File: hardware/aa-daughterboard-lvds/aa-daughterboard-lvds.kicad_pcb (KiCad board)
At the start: 4 copper layers, 175.3 x 96.5 mm, 162 parts, among them CN1 Barrel_Jack, CN10 6P6C, CN11 6P6C, CN12 6P6C, CN13 6P6C, CN14 Conn_01x08, CN15 Conn_01x08, CN16 Conn_01x08, CN17 8P8C, CN18 8P8C, CN19 8P8C, CN2 Conn_01x02, CN3 Conn_01x06, CN4 Conn_01x06, CN5 6P6C, CN6 Conn_01x04, CN7 Conn_01x04, CN8 Conn_01x04, CN9 Conn_01x04, U1 24LC08, U2 NIS5132xx, U3 uA7805, U4 75ALS192, U5 75ALS192, U6 75ALS192, U7 75ALS192, U8 75ALS192

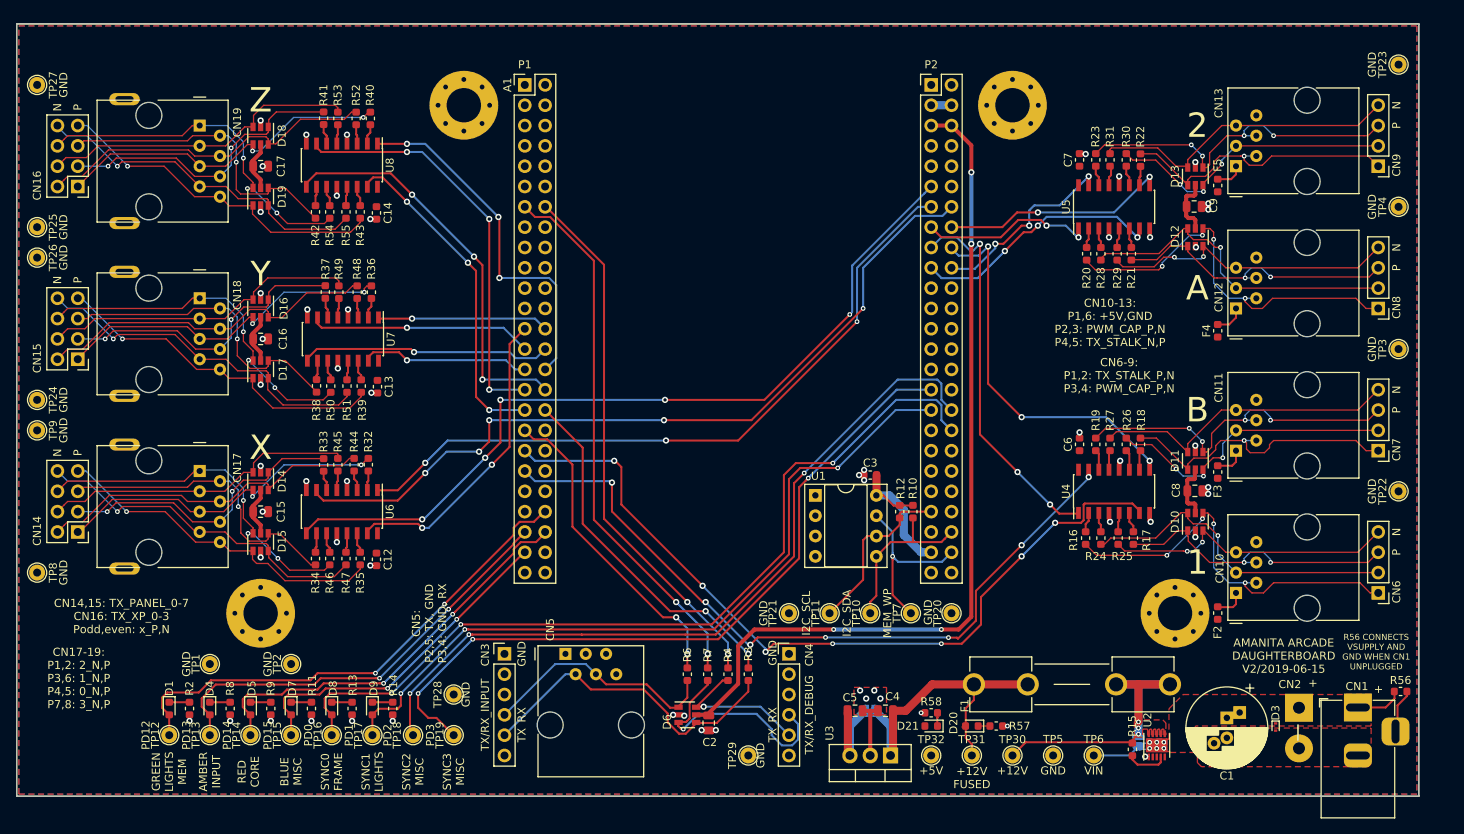
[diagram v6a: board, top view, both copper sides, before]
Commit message: Second rount almost ready, less fiducials
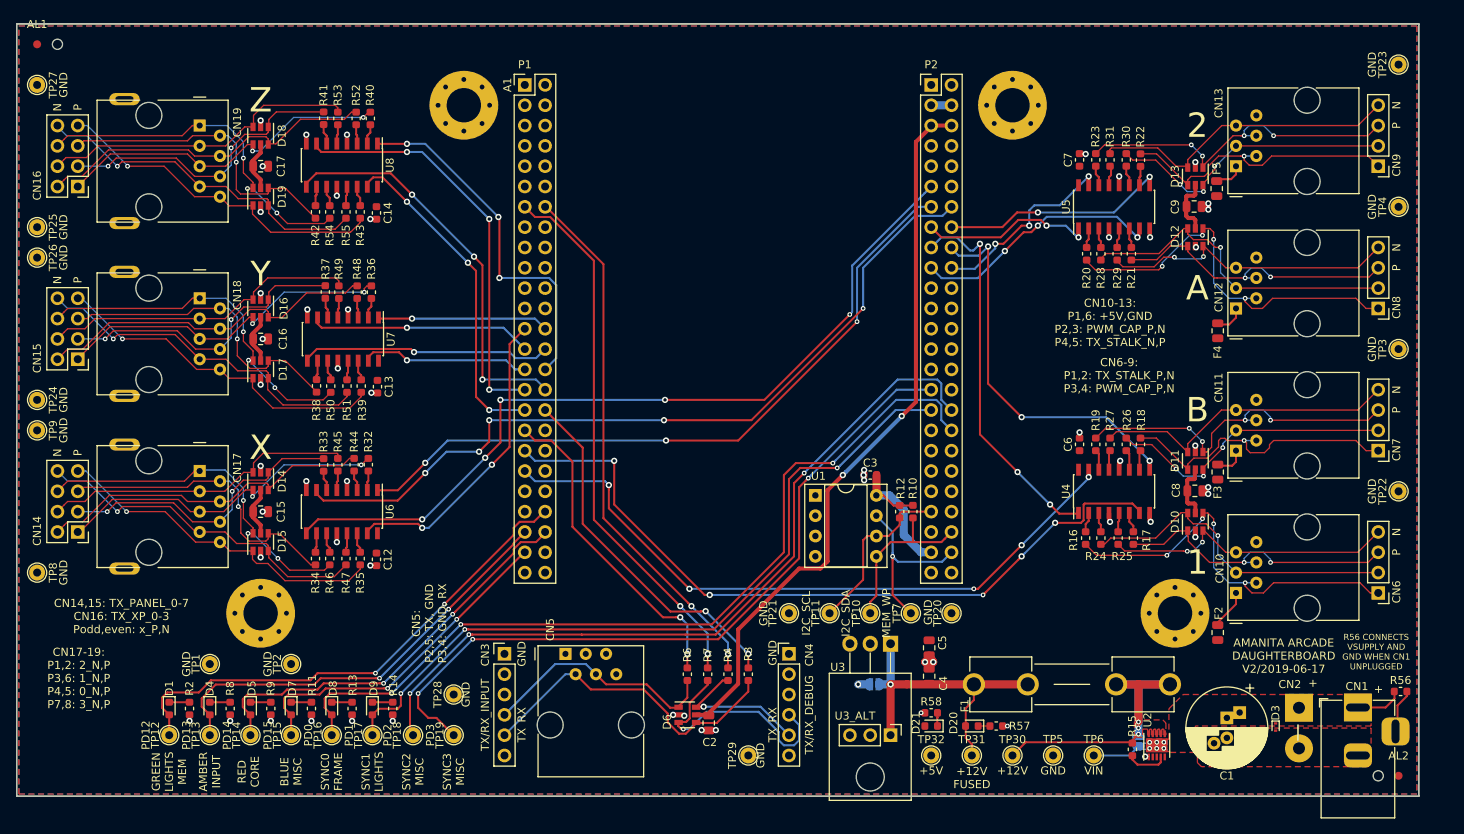
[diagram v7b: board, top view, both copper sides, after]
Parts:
- added AL1: Fiducial_1mm_Dia_2.54mm_Outer_CopperTop, Fiducial:Fiducial_1mm_Dia_2.54mm_Outer_CopperTop, F.Cu at (55.9, 53.3)
- added AL2: Fiducial_1mm_Dia_2.54mm_Outer_CopperTop, Fiducial:Fiducial_1mm_Dia_2.54mm_Outer_CopperTop, F.Cu at (226.1, 144.8)
- added AL5: StencilAlignment_1.27mm, aa-shared:StencilAlignment_1.27mm, F.Cu at (58.4, 53.3)
- added AL6: StencilAlignment_1.27mm, aa-shared:StencilAlignment_1.27mm, F.Cu at (223.5, 144.8)
- added U3_ALT: PinHeader_1x03_P2.54mm_Vertical, Connector_PinHeader_2.54mm:PinHeader_1x03_P2.54mm_Vertical, F.Cu at (162.6, 139.7)
- D10, D11, D12, D13, D14, D15, D16, D17, D18, D19: value D5V0P4UR6SO -> DT1042
- F2, F3, F4, F5: footprint Fuse:Fuse_0603_1608Metric -> Fuse:Fuse_0805_2012Metric
- U3: footprint Package_TO_SOT_THT:TO-220-3_Vertical -> Package_TO_SOT_THT:TO-220-3_Horizontal_TabDown
- moved U3 14.0 mm to (162.6, 128.3)
- moved C5 12.2 mm to (167.4, 128.8), turned to 270 degrees
- moved C4 6.96 mm to (167.4, 132.3), turned to 90 degrees
- moved JP7 3.34 mm to (160.5, 133.3)
- moved F2 2.44 mm to (203.5, 126.9)
- moved F5 0.40 mm to (203.3, 71.4)
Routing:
- net +3V: track 107.2 -> 90.7 mm, vias 4 -> 2
- net +5V: track 48.1 -> 37.3 mm, vias 0 -> 1
- net /PWM_CAP_B: track 93.5 -> 85.0 mm, vias 7 -> 5
- net /PWM_CAP_1: track 101.7 -> 94.0 mm, vias 7 -> 5
- net GND: track 51.6 -> 47.2 mm, vias 60 -> 58
- net Net-(CN10-Pad1): track 3.84 -> 5.14 mm
- net Net-(C4-Pad1): track 40.7 -> 39.7 mm, vias 0 -> 1
- net /PWM_CAP_2_P: track 44.3 -> 43.6 mm
- net /TX_STALK_B_N: track 37.5 -> 36.8 mm
- net /RX_DEBUG_S: track 29.5 -> 30.1 mm
- net /RX_INPUT: track 39.9 -> 40.4 mm
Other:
- board text added: "AMANITA ARCADE DAUGHTERBOARD V2/2019-06-17"
- board text removed: "AMANITA ARCADE DAUGHTERBOARD V2/2019-06-15"

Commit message: Final designs and actual sent gerbers for first for-real run
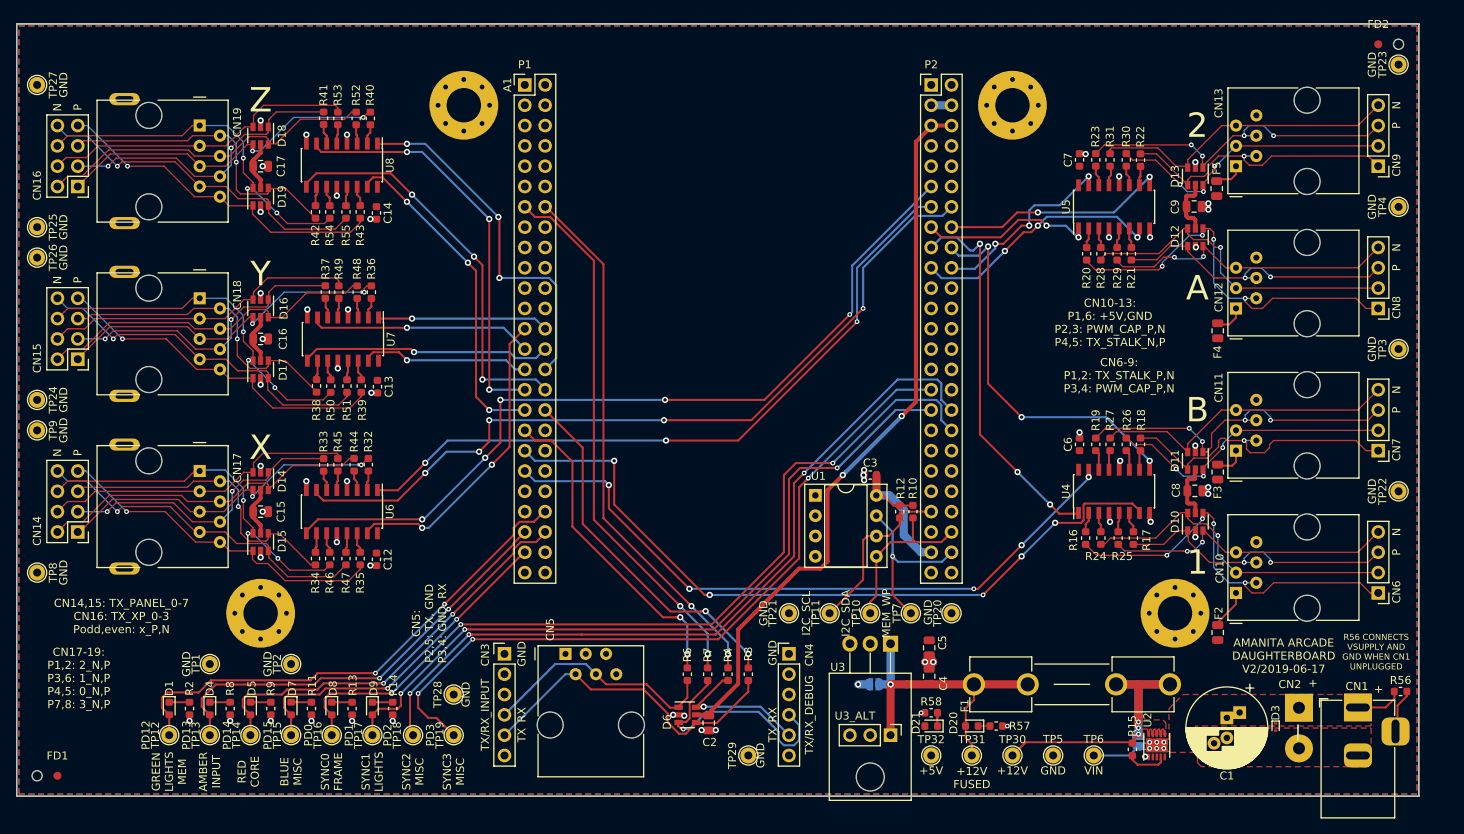
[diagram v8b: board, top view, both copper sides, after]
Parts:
- moved FD1 91.5 mm to (58.4, 144.8)
- moved FD2 91.5 mm to (223.5, 53.3)
- moved FD5 91.5 mm to (55.9, 144.8)
- moved FD6 91.5 mm to (226.1, 53.3)
- renumbered AL1 to FD1, AL2 to FD2, AL5 to FD5, AL6 to FD6
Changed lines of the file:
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@@
   )
   (setup
-    (last_trace_width 1.016)
+    (last_trace_width 0.254)
     (user_trace_width 0.1524)
     (user_trace_width 0.254)
@@
   )
   (module Fiducial:Fiducial_1mm_Dia_2.54mm_Outer_CopperTop (layer F.Cu)
-    (at 226.06 144.78)
+    (at 223.52 53.34)
     (descr "Circular Fiducial, 1mm bare copper top, 2.54mm keepout")
     (tags fiducial)
     (attr smd)
-    (fp_text reference AL2 (at 0 -2.5) (layer F.SilkS)
+    (fp_text reference FD2 (at 0 -2.5) (layer F.SilkS)
       (effects (font (size 1 1) (thickness 0.15)))
     )
@@
   )
   (module aa-shared:StencilAlignment_1.27mm (layer F.Cu)
-    (at 223.52 144.78)
-    (fp_text reference AL6 (at 0 -2.032) (layer F.SilkS) hide
+    (at 226.06 53.34)
+    (fp_text reference FD6 (at 0 -2.032) (layer F.SilkS) hide
       (effects (font (size 1 1) (thickness 0.15)))
     )
@@
   )
   (module aa-shared:StencilAlignment_1.27mm (layer F.Cu)
-    (at 58.42 53.34)
-    (fp_text reference AL5 (at 0 -2.032) (layer F.SilkS) hide
+    (at 55.88 144.78)
+    (fp_text reference FD5 (at 0 -2.032) (layer F.SilkS) hide
       (effects (font (size 1 1) (thickness 0.15)))
     )
@@
   )
   (module Fiducial:Fiducial_1mm_Dia_2.54mm_Outer_CopperTop (layer F.Cu)
-    (at 55.88 53.34)
+    (at 58.42 144.78)
     (descr "Circular Fiducial, 1mm bare copper top, 2.54mm keepout")
     (tags fiducial)
     (attr smd)
-    (fp_text reference AL1 (at 0 -2.5) (layer F.SilkS)
+    (fp_text reference FD1 (at 0 -2.5) (layer F.SilkS)
       (effects (font (size 1 1) (thickness 0.15)))
     )
